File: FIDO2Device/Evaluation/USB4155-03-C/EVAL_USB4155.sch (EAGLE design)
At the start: 2 parts, among them CN2 87520-0010BLF, CN3 IF_5PIN_H

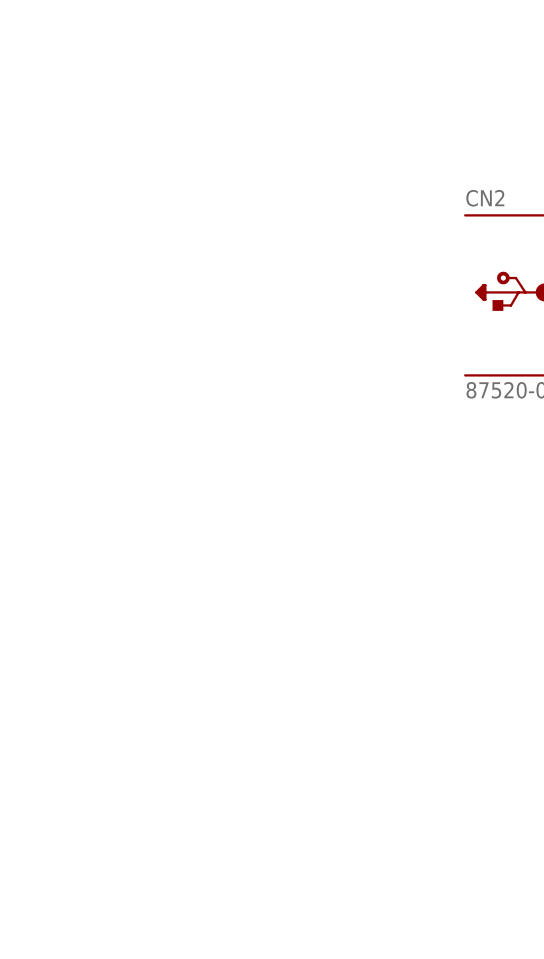
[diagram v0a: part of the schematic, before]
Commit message: 回路図を更新
・コネクター`USB4155-03-C`を回路図に設置
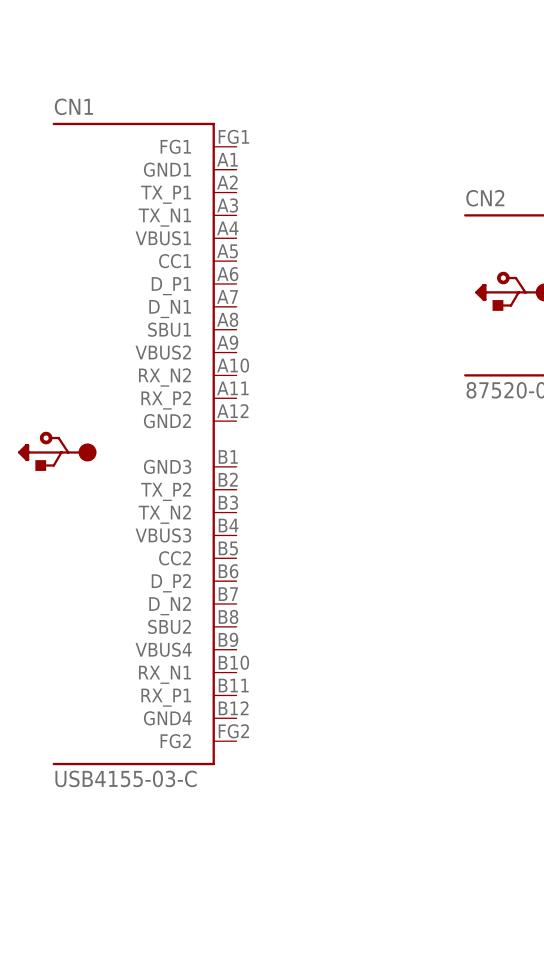
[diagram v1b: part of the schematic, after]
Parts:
- added CN1: USB4155-03-C, Connectors:USB4155-03-C
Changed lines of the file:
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@@
 <part name="CN3" library="Connectors" deviceset="IF_5PIN" device="_H"/>
 <part name="GND3" library="Supply" deviceset="0V" device=""/>
+<part name="CN1" library="Connectors" deviceset="USB4155-03-C" device=""/>
 </parts>
 <sheets>
@@
 <instance part="CN3" gate="G$1" x="139.7" y="66.04"/>
 <instance part="GND3" gate="1" x="134.62" y="48.26"/>
+<instance part="CN1" gate="G$1" x="60.96" y="93.98"/>
 </instances>
 <busses>

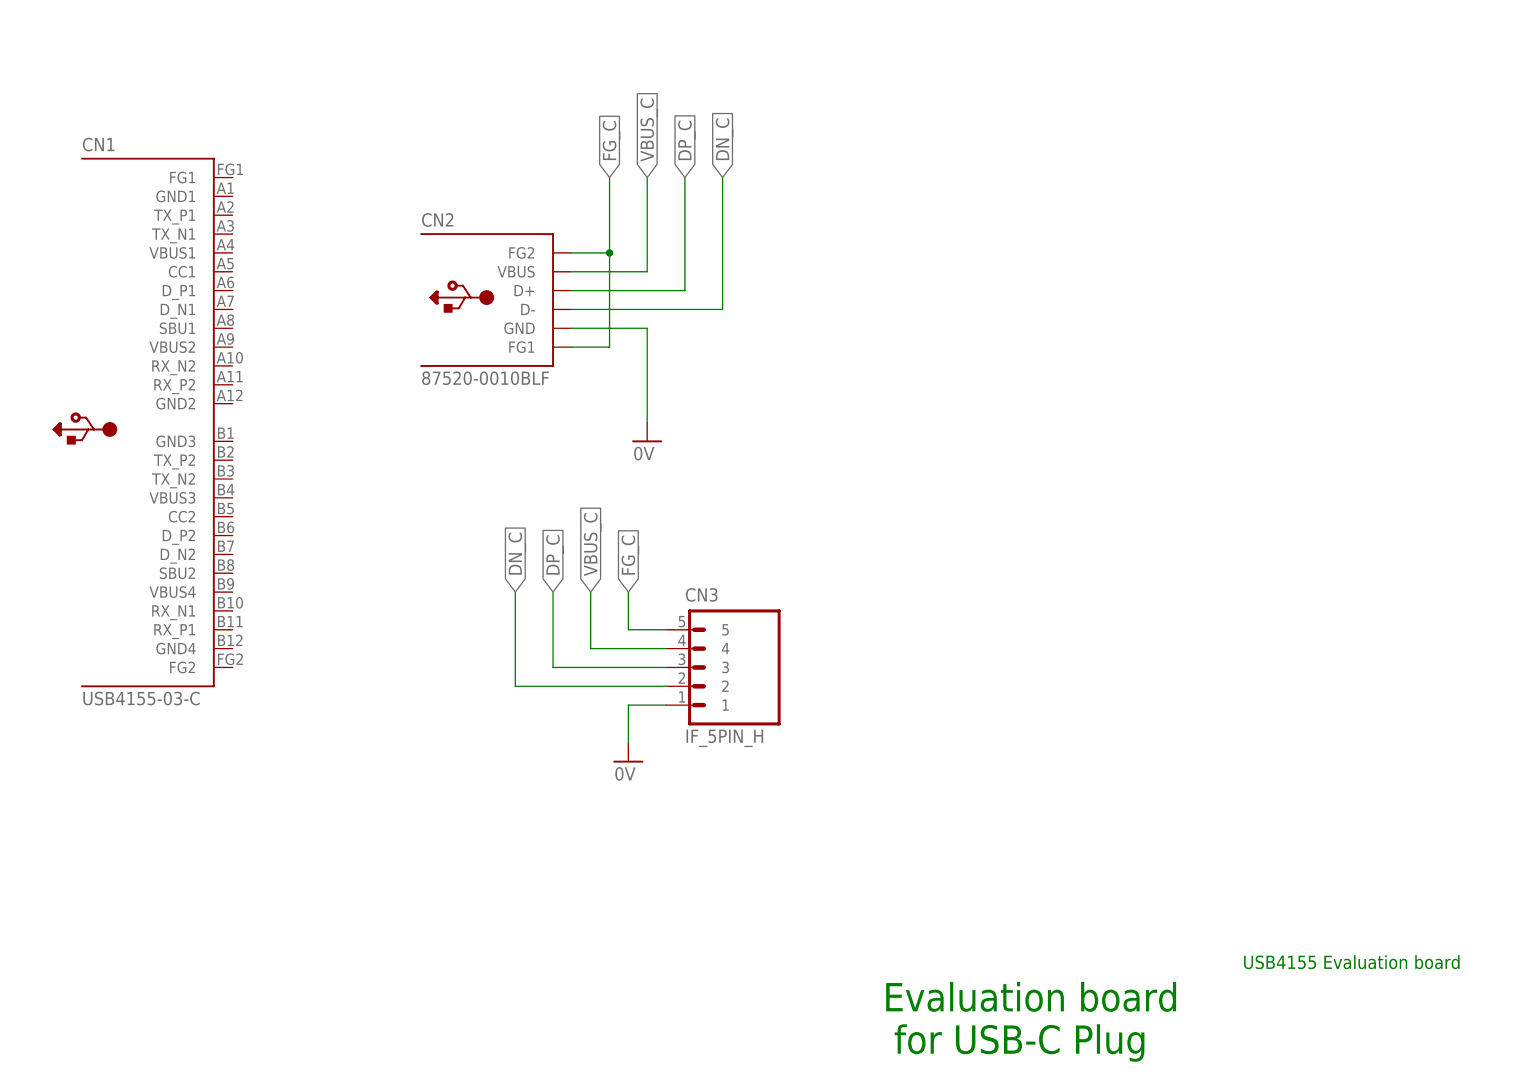
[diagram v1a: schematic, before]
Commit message: 回路図を更新
・コネクター`USB4155-03-C`を、動作確認用コネクター`87520-0010BLF`と接続
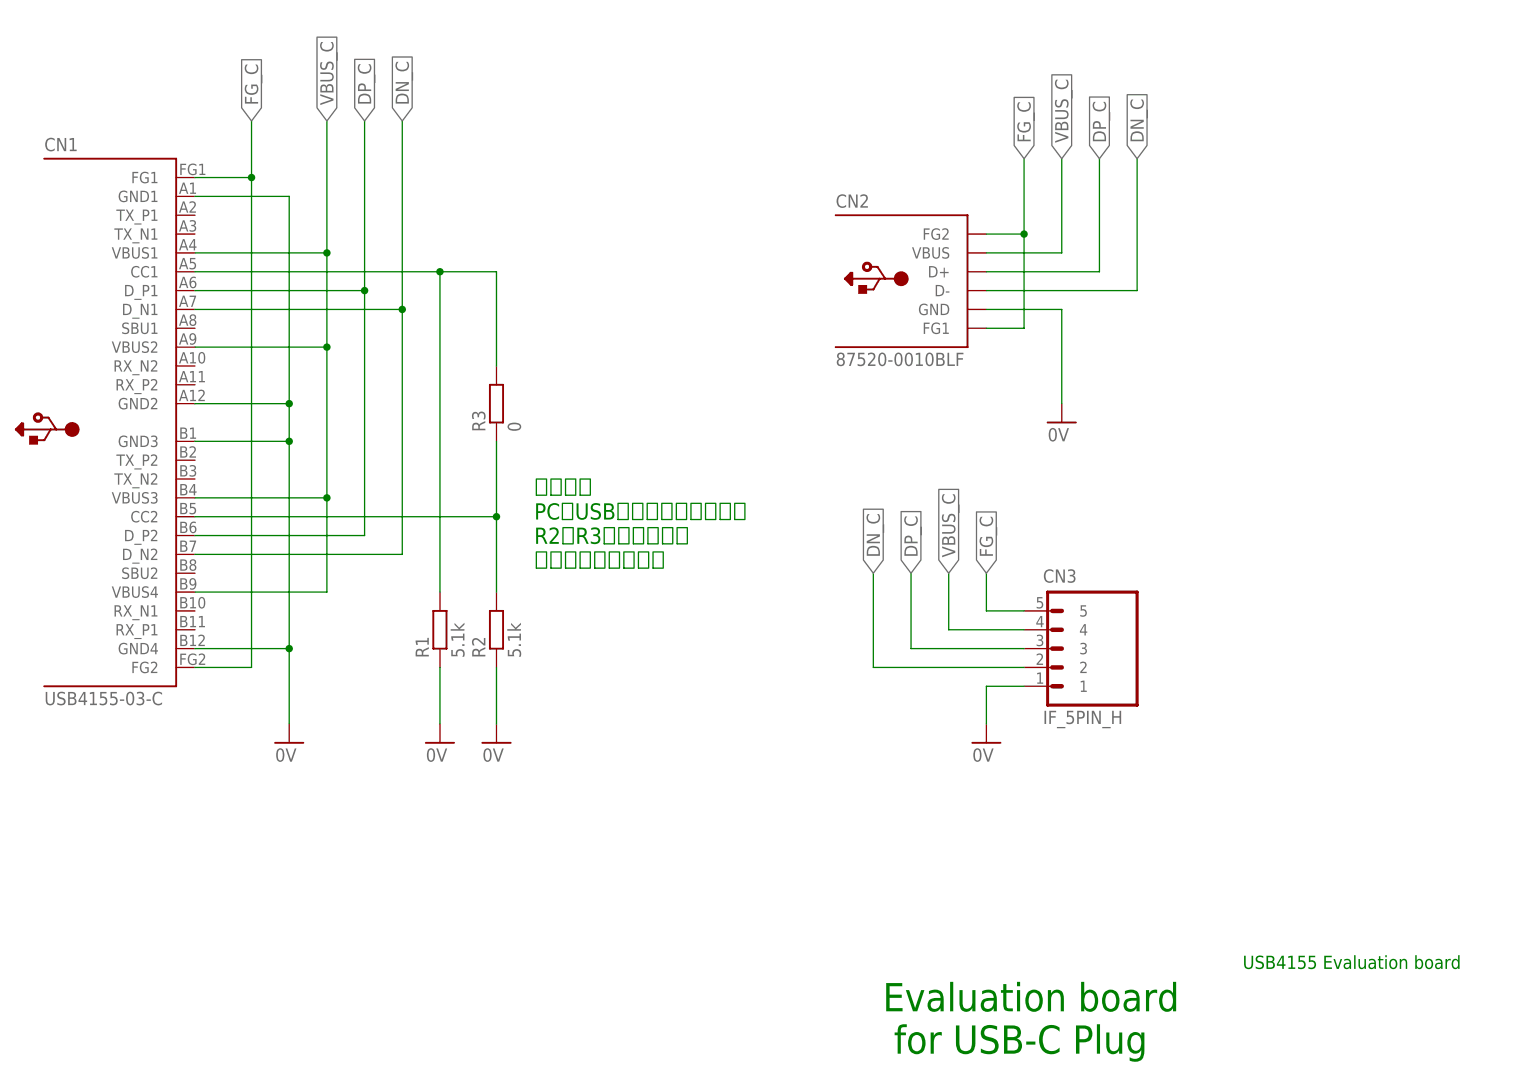
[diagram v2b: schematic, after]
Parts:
- added R1, R2: 5.1k, Parts:RESISTOR_0402N
- added R3: 0, Parts:RESISTOR_0402N
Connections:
- new net N$1: CN1.CC1, R1.2, R3.2
- new net N$2: CN1.CC2, R2.2, R3.1
- net 0V: now also CN1.GND1, CN1.GND2, CN1.GND3, CN1.GND4, R1.1, R2.1
- net DN_C: now also CN1.D_N1, CN1.D_N2
- net DP_C: now also CN1.D_P1, CN1.D_P2
- net FG_C: now also CN1.FG1, CN1.FG2
- net VBUS_C: now also CN1.VBUS1, CN1.VBUS2, CN1.VBUS3, CN1.VBUS4
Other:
- note added: "【注意】 PCのUSBポートに装着時は、 R2、R3のどちらかを 撤去してください。"
- moved on the sheet: CN1, CN2, CN3

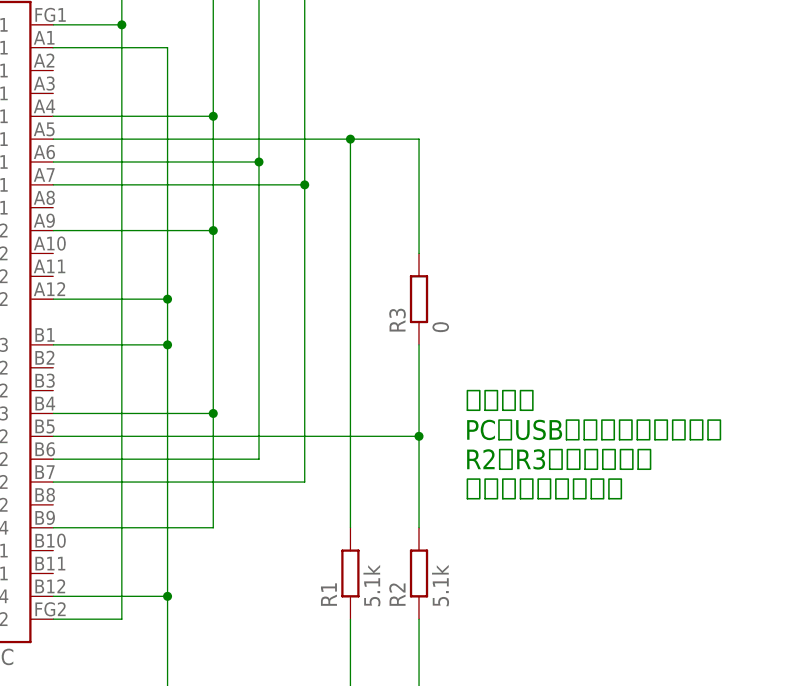
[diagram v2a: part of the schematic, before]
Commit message: レイアウトを更新
・信号線のViaを仮配置
・デザインルールを一部修正
（Drill＝0.2mm、Restring＝0.1mm、Clearance＝0.15mm）
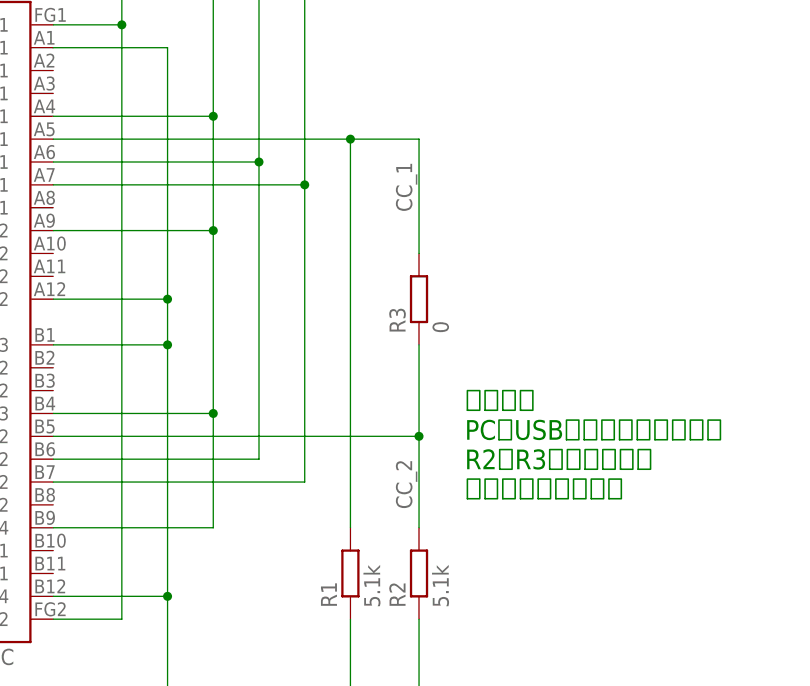
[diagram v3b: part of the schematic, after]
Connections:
- net N$1 renamed CC_1
- net N$2 renamed CC_2
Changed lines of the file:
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@@
 </segment>
 </net>
-<net name="N$1" class="0">
+<net name="CC_1" class="0">
 <segment>
 <pinref part="CN1" gate="G$1" pin="CC1"/>
@@
 <wire x1="109.22" y1="114.3" x2="109.22" y2="71.12" width="0.1524" layer="91"/>
 <junction x="109.22" y="114.3"/>
+<label x="114.3" y="111.76" size="1.778" layer="95" rot="R270"/>
 </segment>
 </net>
-<net name="N$2" class="0">
+<net name="CC_2" class="0">
 <segment>
 <pinref part="CN1" gate="G$1" pin="CC2"/>
@@
 <wire x1="116.84" y1="81.28" x2="116.84" y2="91.44" width="0.1524" layer="91"/>
 <junction x="116.84" y="81.28"/>
+<label x="114.3" y="78.74" size="1.778" layer="95" rot="R270"/>
 </segment>
 </net>
